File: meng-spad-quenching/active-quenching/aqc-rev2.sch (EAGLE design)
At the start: 277 parts, among them IC1 ADCMP582, IC10 74AHC1G04DBV, IC11 74AHC1G04DBV, IC12 TLV272DGK, IC13 TLV271DBV, IC14 74AHC1G04DBV, IC15 ALD1106, IC16 ALD1107, IC17 74AHC1G04DBV, IC18 LT1534-1, IC19 LT1534-1, IC2 TLV271DBV, IC20 STM32F411RE, IC22 TPS7A3001, IC23 74LVT126, IC24 TPS7A4901, IC25 TPS7A4901, IC26 74AHC1G14DBV, IC27 USBLC6-2SC6Y, IC28 MAX572X, IC3 NC7SV74K8X, IC4 TLV272DGK, IC5 NC7WZ16P6X, IC6 LTC1711, IC7 DS1100LU-20+, IC8 LM1117, M1 BSS806N, Q1 IRLML6402TRPBF, Q2 MMBTH81, Q3 MMBTH81, Q5 MMBTH81, Q7 MMBTH81, Q8 MMBTH81, T1 MMBTH10, T2 MMBTH10, T5 MMBTH10, T6 MMBTH10, T7 MMBTH10, T8 MMBTH10, T9 MMBTH10, U1 SN65EPT21DGK, U2 SN65EPT22DGK, U3 TPS78233DDCT, X1 CONN_SPAD, X2 CONN_PHOTON_COUNTER, X6 CONN_FORCE_QUENCH, X7 CONN_PULLDN_SENSE, X8 PN61729-S

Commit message: Added USB inrush limiting
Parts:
- added C109: 4u7, rcl:C-EUC0805
- added C110: 100n, rcl:C-EUC0603
- added C111: 47u, 20V, rcl:CPOL-EUCT7343
- added R68: 100k, resistor:R-EU_R0805
- added R69: 4k7, resistor:R-EU_R0805
- C81: value 47u, 25V -> 4.7u; device rcl:CPOL-EUE2.5-6 -> rcl:C-EUC0805
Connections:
- new net !MCU_SMPS_PWREN: R69.2
- new net N$12: C110.1, Q1.G, R68.1, R69.1
- new net SMPS_USB_VDD: C104.1, C110.2, C111.+, C40.1, C41.1, C45.1, C81.1, IC18.VIN, IC19.VIN, L3.1, L4.1, Q1.D
- net GND: now also C109.2, C111.-, C81.2; no longer C81.-
- net PP_P5V0: no longer R37.2
- net USB_VDD: now also C109.1, Q1.S, R37.2, R68.2; no longer C104.1, C40.1, C41.1, C45.1, C81.+, IC18.VIN, IC19.VIN, L3.1, L4.1
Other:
- note added: "USB INPUT AND INRUSH LIMITING"
- note added: "USB Inrush Limiting: See pg. 7 of FTDI AN_146"

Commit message: misc routing
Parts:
- added L7, L8: 25n, meng:INDUCTOR0603
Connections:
- net N$53 renamed BOOST_SW_NODE
- new net N$19: IC18.PGND, L7.P$1
- new net N$20: IC19.PGND, L8.P$1
- net GND: now also L7.P$2, L8.P$2; no longer IC18.PGND, IC19.PGND
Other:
- note removed: "25nH"
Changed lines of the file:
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@@
 <part name="GND158" library="supply1" deviceset="GND" device=""/>
 <part name="C111" library="rcl" deviceset="CPOL-EU" device="CT7343" value="47u, 20V"/>
+<part name="L7" library="meng" deviceset="INDUCTOR" device="0603" value="25n"/>
+<part name="L8" library="meng" deviceset="INDUCTOR" device="0603" value="25n"/>
 </parts>
 <sheets>
@@
 <text x="266.7" y="8.255" size="2.54" layer="97" font="vector" align="center">2.0</text>
 <text x="223.52" y="8.255" size="3.81" layer="97" font="vector" align="center">1 of 1</text>
-<text x="121.92" y="137.16" size="1.778" layer="98">25nH</text>
 <text x="182.88" y="127" size="1.778" layer="98">Select filter order</text>
 <text x="172.72" y="177.8" size="1.778" layer="98">Bypass 2nd stage filter</text>
@@
 <instance part="GND127" gate="1" x="66.04" y="154.94"/>
 <instance part="C81" gate="G$1" x="66.04" y="165.1"/>
+<instance part="L7" gate="G$1" x="127" y="134.62" smashed="yes">
+<attribute name="NAME" x="116.84" y="137.16" size="1.778" layer="95"/>
+<attribute name="VALUE" x="127" y="137.16" size="1.778" layer="97"/>
+</instance>
 </instances>
 <busses>
@@
 <wire x1="134.62" y1="127" x2="134.62" y2="119.38" width="0.1524" layer="91"/>
 <junction x="134.62" y="119.38"/>
-<wire x1="109.22" y1="134.62" x2="119.38" y2="134.62" width="0.1524" layer="91"/>
-<wire x1="119.38" y1="134.62" x2="134.62" y2="134.62" width="0.1524" layer="91"/>
-<wire x1="134.62" y1="134.62" x2="134.62" y2="142.24" width="0.1524" layer="91"/>
 <wire x1="134.62" y1="127" x2="134.62" y2="134.62" width="0.1524" layer="91"/>
 <junction x="134.62" y="127"/>
-<junction x="134.62" y="134.62"/>
-<wire x1="118.11" y1="135.89" x2="119.38" y2="134.62" width="0.1524" layer="91" curve="90"/>
-<wire x1="118.11" y1="135.89" x2="119.38" y2="137.16" width="0.1524" layer="91" curve="-90"/>
-<wire x1="120.65" y1="135.89" x2="119.38" y2="137.16" width="0.1524" layer="91" curve="90"/>
-<wire x1="120.65" y1="135.89" x2="119.38" y2="134.62" width="0.1524" layer="91" curve="-90"/>
-<pinref part="IC18" gate="G$1" pin="PGND"/>
 <pinref part="R42" gate="G$1" pin="2"/>
 <pinref part="R43" gate="G$1" pin="2"/>
 <pinref part="C68" gate="G$1" pin="1"/>
 <pinref part="GND125" gate="1" pin="GND"/>
+<pinref part="L7" gate="G$1" pin="P$2"/>
+<wire x1="134.62" y1="134.62" x2="134.62" y2="142.24" width="0.1524" layer="91"/>
+<wire x1="129.54" y1="134.62" x2="134.62" y2="134.62" width="0.1524" layer="91"/>
+<junction x="134.62" y="134.62"/>
 </segment>
 <segment>
@@
 </segment>
 </net>
-<net name="N$53" class="0">
+<net name="BOOST_SW_NODE" class="0">
 <segment>
 <wire x1="109.22" y1="142.24" x2="111.76" y2="142.24" width="0.1524" layer="91"/>
@@
 </segment>
 </net>
+<net name="N$19" class="0">
+<segment>
+<pinref part="IC18" gate="G$1" pin="PGND"/>
+<pinref part="L7" gate="G$1" pin="P$1"/>
+<wire x1="109.22" y1="134.62" x2="119.38" y2="134.62" width="0.1524" layer="91"/>
+</segment>
+</net>
 </nets>
 </sheet>
@@
 <text x="266.7" y="8.255" size="2.54" layer="97" font="vector" align="center">2.0</text>
 <text x="223.52" y="8.255" size="3.81" layer="97" font="vector" align="center">1 of 1</text>
-<text x="147.32" y="129.54" size="1.778" layer="98">25nH</text>
 <text x="124.46" y="96.52" size="1.778" layer="98">-2.5V Nom.</text>
 <text x="167.64" y="167.64" size="1.778" layer="98">Coupling Cap Possible Alternate PN: RNU1C101MDS1JX</text>
@@
 <instance part="C45" gate="G$1" x="127" y="152.4"/>
 <instance part="GND69" gate="1" x="127" y="142.24"/>
+<instance part="L8" gate="G$1" x="152.4" y="127" smashed="yes">
+<attribute name="NAME" x="142.24" y="129.54" size="1.778" layer="95"/>
+<attribute name="VALUE" x="152.4" y="129.54" size="1.778" layer="97"/>
+</instance>
 </instances>
 <busses>
@@
 <wire x1="160.02" y1="119.38" x2="160.02" y2="111.76" width="0.1524" layer="91"/>
 <junction x="160.02" y="111.76"/>
-<wire x1="134.62" y1="127" x2="144.78" y2="127" width="0.1524" layer="91"/>
-<wire x1="144.78" y1="127" x2="160.02" y2="127" width="0.1524" layer="91"/>
-<wire x1="160.02" y1="127" x2="160.02" y2="134.62" width="0.1524" layer="91"/>
 <wire x1="160.02" y1="119.38" x2="160.02" y2="127" width="0.1524" layer="91"/>
 <junction x="160.02" y="119.38"/>
-<junction x="160.02" y="127"/>
-<wire x1="143.51" y1="128.27" x2="144.78" y2="127" width="0.1524" layer="91" curve="90"/>
-<wire x1="143.51" y1="128.27" x2="144.78" y2="129.54" width="0.1524" layer="91" curve="-90"/>
-<wire x1="146.05" y1="128.27" x2="144.78" y2="129.54" width="0.1524" layer="91" curve="90"/>
-<wire x1="146.05" y1="128.27" x2="144.78" y2="127" width="0.1524" layer="91" curve="-90"/>
-<pinref part="IC19" gate="G$1" pin="PGND"/>
 <pinref part="GND53" gate="1" pin="GND"/>
 <pinref part="C43" gate="G$1" pin="2"/>
 <pinref part="R58" gate="G$1" pin="2"/>
 <pinref part="R59" gate="G$1" pin="2"/>
+<pinref part="L8" gate="G$1" pin="P$2"/>
+<wire x1="160.02" y1="127" x2="160.02" y2="134.62" width="0.1524" layer="91"/>
+<wire x1="154.94" y1="127" x2="160.02" y2="127" width="0.1524" layer="91"/>
+<junction x="160.02" y="127"/>
 </segment>
 <segment>
@@
 </segment>
 </net>
+<net name="N$20" class="0">
+<segment>
+<pinref part="L8" gate="G$1" pin="P$1"/>
+<pinref part="IC19" gate="G$1" pin="PGND"/>
+<wire x1="144.78" y1="127" x2="134.62" y2="127" width="0.1524" layer="91"/>
+</segment>
+</net>

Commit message: misc routing
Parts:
- C25, C26, C29, C87, C88: device rcl:C-EUC0402 -> rcl:C-EUC0603
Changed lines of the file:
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@@
 <part name="DNP58" library="meng" deviceset="ARROW_1DIR" device=""/>
 <part name="R33" library="rcl" deviceset="R-EU_" device="R0603" value="47R"/>
-<part name="C25" library="rcl" deviceset="C-EU" device="C0402" value="100n"/>
-<part name="C26" library="rcl" deviceset="C-EU" device="C0402" value="100n"/>
-<part name="C29" library="rcl" deviceset="C-EU" device="C0402" value="100n"/>
-<part name="C87" library="rcl" deviceset="C-EU" device="C0402" value="4.7u"/>
+<part name="C25" library="rcl" deviceset="C-EU" device="C0603" value="100n"/>
+<part name="C26" library="rcl" deviceset="C-EU" device="C0603" value="100n"/>
+<part name="C29" library="rcl" deviceset="C-EU" device="C0603" value="100n"/>
+<part name="C87" library="rcl" deviceset="C-EU" device="C0603" value="4.7u"/>
 <part name="GND33" library="supply1" deviceset="GND" device=""/>
 <part name="GND48" library="supply1" deviceset="GND" device=""/>
@@
 <part name="DNP79" library="meng" deviceset="ARROW_1DIR" device=""/>
 <part name="DNP93" library="meng" deviceset="ARROW_1DIR" device=""/>
-<part name="C88" library="rcl" deviceset="C-EU" device="C0402" value="100n"/>
+<part name="C88" library="rcl" deviceset="C-EU" device="C0603" value="100n"/>
 <part name="GND72" library="supply1" deviceset="GND" device=""/>
 <part name="DNP94" library="meng" deviceset="ARROW_1DIR" device=""/>

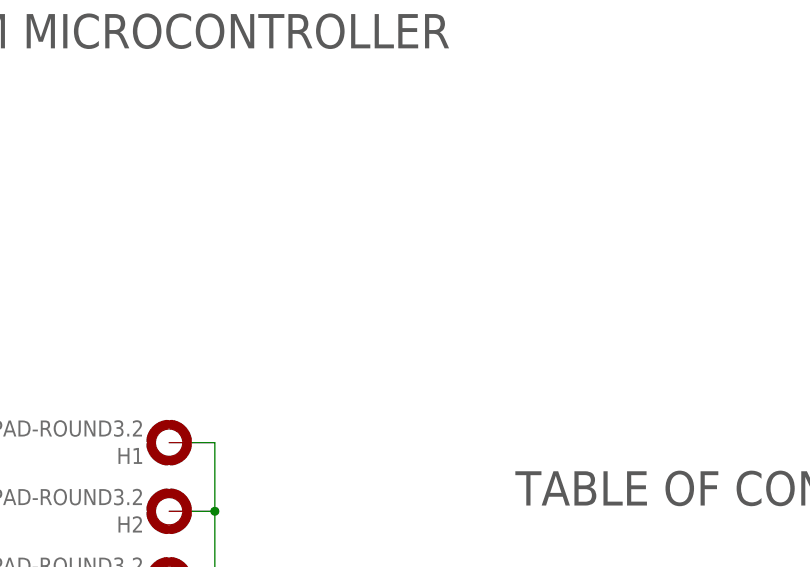
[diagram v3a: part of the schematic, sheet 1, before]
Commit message: Added 4-40 Keystone RA, Arranged Right Side Conns.
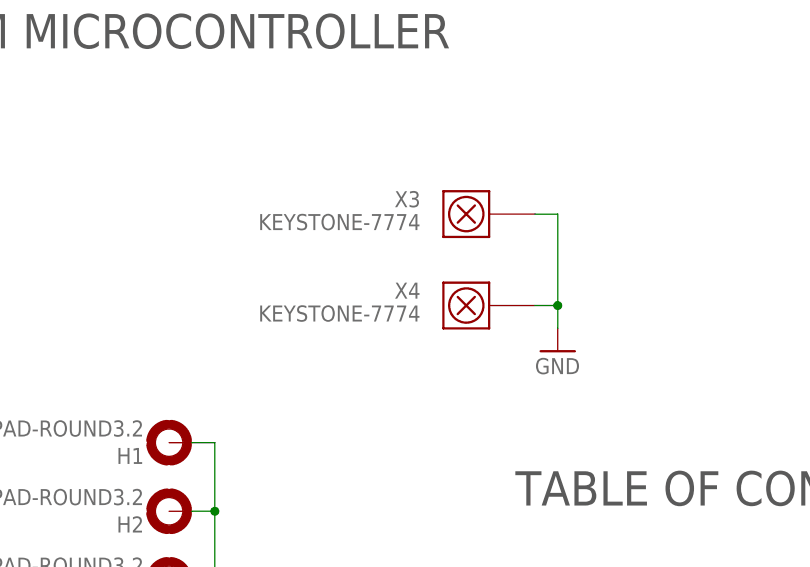
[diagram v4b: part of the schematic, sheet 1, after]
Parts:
- added X3, X4: KEYSTONE-7774, meng:KEYSTONE-7774
- R36, R73: device resistor:R-EU_R0603 -> resistor:R-EU_R0402
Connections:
- net GND: now also X3.1, X4.1
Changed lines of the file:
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@@
 <setting verticaltext="up"/>
 </settings>
-<grid distance="0.1" unitdist="inch" unit="inch" style="lines" multiple="1" display="yes" altdistance="0.01" altunitdist="inch" altunit="inch"/>
+<grid distance="0.1" unitdist="inch" unit="inch" style="lines" multiple="1" display="no" altdistance="0.01" altunitdist="inch" altunit="inch"/>
 <layers>
 <layer number="1" name="Top" color="4" fill="1" visible="yes" active="no"/>
@@
 <part name="GND114" library="supply1" deviceset="GND" device=""/>
 <part name="C90" library="rcl" deviceset="C-EU" device="C0402" value="100n"/>
-<part name="R36" library="resistor" deviceset="R-EU_" device="R0603" value="22R"/>
-<part name="R73" library="resistor" deviceset="R-EU_" device="R0603" value="22R"/>
+<part name="R36" library="resistor" deviceset="R-EU_" device="R0402" value="22R"/>
+<part name="R73" library="resistor" deviceset="R-EU_" device="R0402" value="22R"/>
 <part name="C91" library="rcl" deviceset="C-EU" device="C0402" value="47p"/>
 <part name="C92" library="rcl" deviceset="C-EU" device="C0402" value="47p"/>
@@
 <part name="L7" library="meng" deviceset="INDUCTOR" device="0603" value="25n"/>
 <part name="L8" library="meng" deviceset="INDUCTOR" device="0603" value="25n"/>
+<part name="X3" library="meng" deviceset="KEYSTONE-7774" device="" value="KEYSTONE-7774"/>
+<part name="X4" library="meng" deviceset="KEYSTONE-7774" device="" value="KEYSTONE-7774"/>
+<part name="GND159" library="supply1" deviceset="GND" device=""/>
 </parts>
 <sheets>
@@
 <attribute name="VALUE" x="162.56" y="5.08" size="1.778" layer="96"/>
 </instance>
+<instance part="X3" gate="G$1" x="195.58" y="60.96" smashed="yes" rot="R180">
+<attribute name="NAME" x="187.96" y="63.5" size="1.778" layer="95" rot="R180"/>
+<attribute name="VALUE" x="187.96" y="60.96" size="1.778" layer="96" rot="R180"/>
+</instance>
+<instance part="X4" gate="G$1" x="195.58" y="50.8" smashed="yes" rot="R180">
+<attribute name="NAME" x="187.96" y="53.34" size="1.778" layer="95" rot="R180"/>
+<attribute name="VALUE" x="187.96" y="50.8" size="1.778" layer="96" rot="R180"/>
+</instance>
+<instance part="GND159" gate="1" x="203.2" y="45.72" smashed="yes">
+<attribute name="VALUE" x="200.66" y="43.18" size="1.778" layer="96"/>
+</instance>
 </instances>
 <busses>
@@
 <junction x="165.1" y="27.94"/>
 </segment>
+<segment>
+<pinref part="X4" gate="G$1" pin="1"/>
+<wire x1="200.66" y1="50.8" x2="203.2" y2="50.8" width="0.1524" layer="91"/>
+<pinref part="GND159" gate="1" pin="GND"/>
+<wire x1="203.2" y1="50.8" x2="203.2" y2="48.26" width="0.1524" layer="91"/>
+<wire x1="203.2" y1="50.8" x2="203.2" y2="60.96" width="0.1524" layer="91"/>
+<pinref part="X3" gate="G$1" pin="1"/>
+<wire x1="203.2" y1="60.96" x2="200.66" y2="60.96" width="0.1524" layer="91"/>
+<junction x="203.2" y="50.8"/>
+</segment>
 </net>

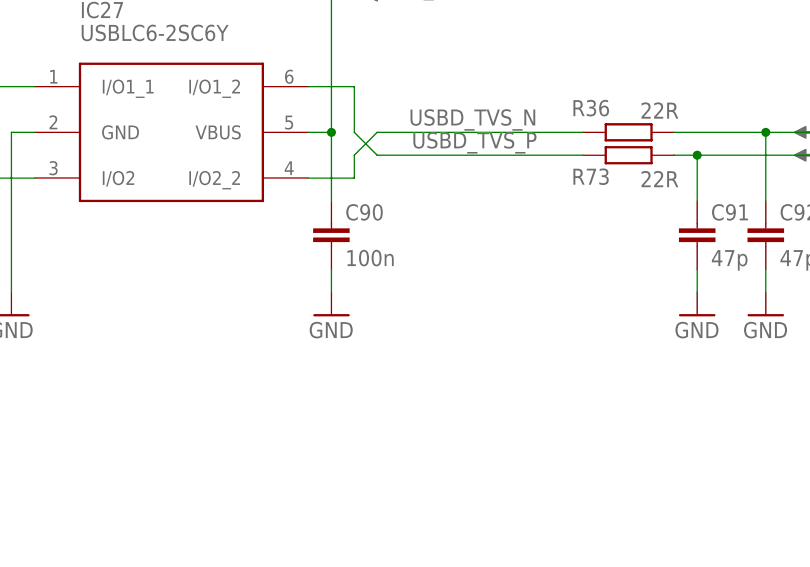
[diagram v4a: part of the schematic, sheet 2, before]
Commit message: Started placement of starved inverters
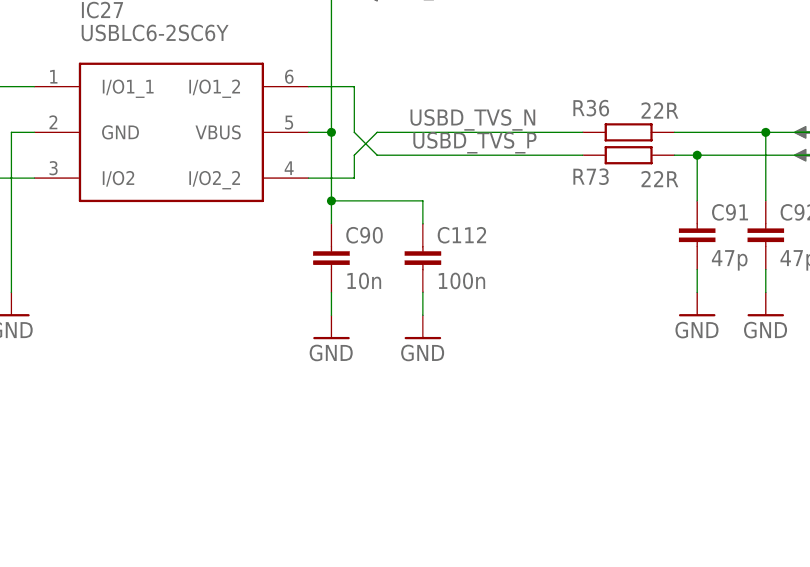
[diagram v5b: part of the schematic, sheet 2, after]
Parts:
- added C112: 100n, rcl:C-EUC0402
- C107, C52: device rcl:C-EUC0402 -> rcl:C-EUC0603
- C90: value 100n -> 10n
- D1: value SD101BW-TP -> BAS40; device diode:DIODE-SOD123 -> diode:BAS40
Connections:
- net GND: now also C112.2
- net PP_P3V3: now also C112.1
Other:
- moved on the sheet: C90
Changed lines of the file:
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@@
 <setting verticaltext="up"/>
 </settings>
-<grid distance="0.1" unitdist="inch" unit="inch" style="lines" multiple="1" display="no" altdistance="0.01" altunitdist="inch" altunit="inch"/>
+<grid distance="0.1" unitdist="inch" unit="inch" style="lines" multiple="1" display="yes" altdistance="0.01" altunitdist="inch" altunit="inch"/>
 <layers>
 <layer number="1" name="Top" color="4" fill="1" visible="yes" active="no"/>
@@
 <part name="GND79" library="supply1" deviceset="GND" device=""/>
 <part name="R27" library="rcl" deviceset="R-EU_" device="R0603" value="49R9"/>
-<part name="D1" library="diode" deviceset="DIODE-" device="SOD123" value="SD101BW-TP"/>
 <part name="DNP68" library="meng" deviceset="ARROW_1DIR" device=""/>
 <part name="C14" library="rcl" deviceset="C-EU" device="C0603" value="100n"/>
@@
 <part name="IC11" library="74xx-little-de" deviceset="74*1G04" device="DBV" technology="AHC"/>
 <part name="GND89" library="supply1" deviceset="GND" device=""/>
-<part name="C52" library="rcl" deviceset="C-EU" device="C0402" value="10p"/>
+<part name="C52" library="rcl" deviceset="C-EU" device="C0603" value="10p"/>
 <part name="R45" library="rcl" deviceset="R-EU_" device="R0603" value="DNP"/>
 <part name="R46" library="rcl" deviceset="R-EU_" device="R0603" value="0R"/>
@@
 <part name="GND112" library="supply1" deviceset="GND" device=""/>
 <part name="GND114" library="supply1" deviceset="GND" device=""/>
-<part name="C90" library="rcl" deviceset="C-EU" device="C0402" value="100n"/>
+<part name="C90" library="rcl" deviceset="C-EU" device="C0402" value="10n"/>
 <part name="R36" library="resistor" deviceset="R-EU_" device="R0402" value="22R"/>
 <part name="R73" library="resistor" deviceset="R-EU_" device="R0402" value="22R"/>
@@
 <part name="C105" library="rcl" deviceset="C-EU" device="C0603" value="100n"/>
 <part name="C106" library="rcl" deviceset="C-EU" device="C0805" value="10u"/>
-<part name="C107" library="rcl" deviceset="C-EU" device="C0402" value="10n"/>
+<part name="C107" library="rcl" deviceset="C-EU" device="C0603" value="10n"/>
 <part name="GND155" library="supply1" deviceset="GND" device=""/>
 <part name="C108" library="rcl" deviceset="C-EU" device="C0402" value="100n"/>
@@
 <part name="X4" library="meng" deviceset="KEYSTONE-7774" device="" value="KEYSTONE-7774"/>
 <part name="GND159" library="supply1" deviceset="GND" device=""/>
+<part name="C112" library="rcl" deviceset="C-EU" device="C0402" value="100n"/>
+<part name="GND160" library="supply1" deviceset="GND" device=""/>
+<part name="D1" library="diode" deviceset="BAS40" device=""/>
 </parts>
 <sheets>
@@
 <instance part="IC27" gate="G$1" x="127" y="86.36"/>
 <instance part="GND112" gate="1" x="119.38" y="73.66"/>
-<instance part="GND114" gate="1" x="154.94" y="73.66" smashed="yes">
-<attribute name="VALUE" x="152.4" y="71.12" size="1.778" layer="96"/>
+<instance part="GND114" gate="1" x="154.94" y="71.12" smashed="yes">
+<attribute name="VALUE" x="152.4" y="68.58" size="1.778" layer="96"/>
 </instance>
-<instance part="C90" gate="G$1" x="154.94" y="83.82" smashed="yes">
-<attribute name="NAME" x="156.464" y="84.201" size="1.778" layer="95"/>
-<attribute name="VALUE" x="156.464" y="79.121" size="1.778" layer="96"/>
+<instance part="C90" gate="G$1" x="154.94" y="81.28" smashed="yes">
+<attribute name="NAME" x="156.464" y="81.661" size="1.778" layer="95"/>
+<attribute name="VALUE" x="156.464" y="76.581" size="1.778" layer="96"/>
 </instance>
 <instance part="R36" gate="G$1" x="187.96" y="93.98" smashed="yes" rot="MR0">
@@
 <attribute name="VALUE" x="178.943" y="163.0426" size="1.778" layer="96"/>
 </instance>
+<instance part="C112" gate="G$1" x="165.1" y="81.28" smashed="yes">
+<attribute name="NAME" x="166.624" y="81.661" size="1.778" layer="95"/>
+<attribute name="VALUE" x="166.624" y="76.581" size="1.778" layer="96"/>
+</instance>
+<instance part="GND160" gate="1" x="165.1" y="71.12" smashed="yes">
+<attribute name="VALUE" x="162.56" y="68.58" size="1.778" layer="96"/>
+</instance>
 </instances>
 <busses>
@@
 <pinref part="GND114" gate="1" pin="GND"/>
 <pinref part="C90" gate="G$1" pin="2"/>
-<wire x1="154.94" y1="76.2" x2="154.94" y2="78.74" width="0.1524" layer="91"/>
+<wire x1="154.94" y1="73.66" x2="154.94" y2="76.2" width="0.1524" layer="91"/>
 </segment>
 <segment>
@@
 <pinref part="C111" gate="G$1" pin="-"/>
 </segment>
+<segment>
+<pinref part="GND160" gate="1" pin="GND"/>
+<pinref part="C112" gate="G$1" pin="2"/>
+<wire x1="165.1" y1="73.66" x2="165.1" y2="76.2" width="0.1524" layer="91"/>
+</segment>
 </net>
 <net name="USBD_CONN_N" class="1">
@@
 <label x="162.56" y="109.22" size="1.778" layer="95"/>
 <pinref part="C90" gate="G$1" pin="1"/>
-<wire x1="154.94" y1="86.36" x2="154.94" y2="93.98" width="0.1524" layer="91"/>
+<wire x1="154.94" y1="83.82" x2="154.94" y2="86.36" width="0.1524" layer="91"/>
 <junction x="154.94" y="93.98"/>
+<pinref part="C112" gate="G$1" pin="1"/>
+<wire x1="154.94" y1="86.36" x2="154.94" y2="93.98" width="0.1524" layer="91"/>
+<wire x1="165.1" y1="83.82" x2="165.1" y2="86.36" width="0.1524" layer="91"/>
+<wire x1="165.1" y1="86.36" x2="154.94" y2="86.36" width="0.1524" layer="91"/>
+<junction x="154.94" y="86.36"/>
 </segment>
 <segment>
@@
 <attribute name="VALUE" x="80.01" y="121.158" size="1.778" layer="96" rot="MR0"/>
 </instance>
-<instance part="D1" gate="G$1" x="76.2" y="132.08" smashed="yes">
-<attribute name="NAME" x="68.58" y="137.6426" size="1.778" layer="95"/>
-<attribute name="VALUE" x="68.58" y="134.8486" size="1.778" layer="96"/>
-</instance>
 <instance part="DNP68" gate="G$1" x="198.12" y="132.08" smashed="yes" rot="R180"/>
 <instance part="TP1" gate="G$1" x="119.38" y="152.4" smashed="yes">
@@
 </instance>
 <instance part="DNP112" gate="G$1" x="238.76" y="132.08" smashed="yes"/>
+<instance part="D1" gate="1" x="76.2" y="134.62"/>
 </instances>
 <busses>
@@
 <pinref part="R27" gate="G$1" pin="1"/>
 <wire x1="55.88" y1="124.46" x2="68.58" y2="124.46" width="0.1524" layer="91"/>
-<pinref part="D1" gate="G$1" pin="A"/>
 <wire x1="68.58" y1="124.46" x2="71.12" y2="124.46" width="0.1524" layer="91"/>
-<wire x1="73.66" y1="132.08" x2="68.58" y2="132.08" width="0.1524" layer="91"/>
-<wire x1="68.58" y1="132.08" x2="68.58" y2="124.46" width="0.1524" layer="91"/>
+<wire x1="68.58" y1="134.62" x2="68.58" y2="124.46" width="0.1524" layer="91"/>
 <junction x="68.58" y="124.46"/>
+<pinref part="D1" gate="1" pin="A"/>
+<wire x1="68.58" y1="134.62" x2="73.66" y2="134.62" width="0.1524" layer="91"/>
 </segment>
 </net>
@@
 <pinref part="M1" gate="G$1" pin="G"/>
 <wire x1="81.28" y1="124.46" x2="83.82" y2="124.46" width="0.1524" layer="91"/>
-<pinref part="D1" gate="G$1" pin="C"/>
 <wire x1="83.82" y1="124.46" x2="91.44" y2="124.46" width="0.1524" layer="91"/>
-<wire x1="78.74" y1="132.08" x2="83.82" y2="132.08" width="0.1524" layer="91"/>
-<wire x1="83.82" y1="132.08" x2="83.82" y2="124.46" width="0.1524" layer="91"/>
+<wire x1="83.82" y1="134.62" x2="83.82" y2="124.46" width="0.1524" layer="91"/>
 <junction x="83.82" y="124.46"/>
+<pinref part="D1" gate="1" pin="C"/>
+<wire x1="78.74" y1="134.62" x2="83.82" y2="134.62" width="0.1524" layer="91"/>
 </segment>
 </net>
